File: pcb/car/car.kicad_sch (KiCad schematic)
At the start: 9 parts

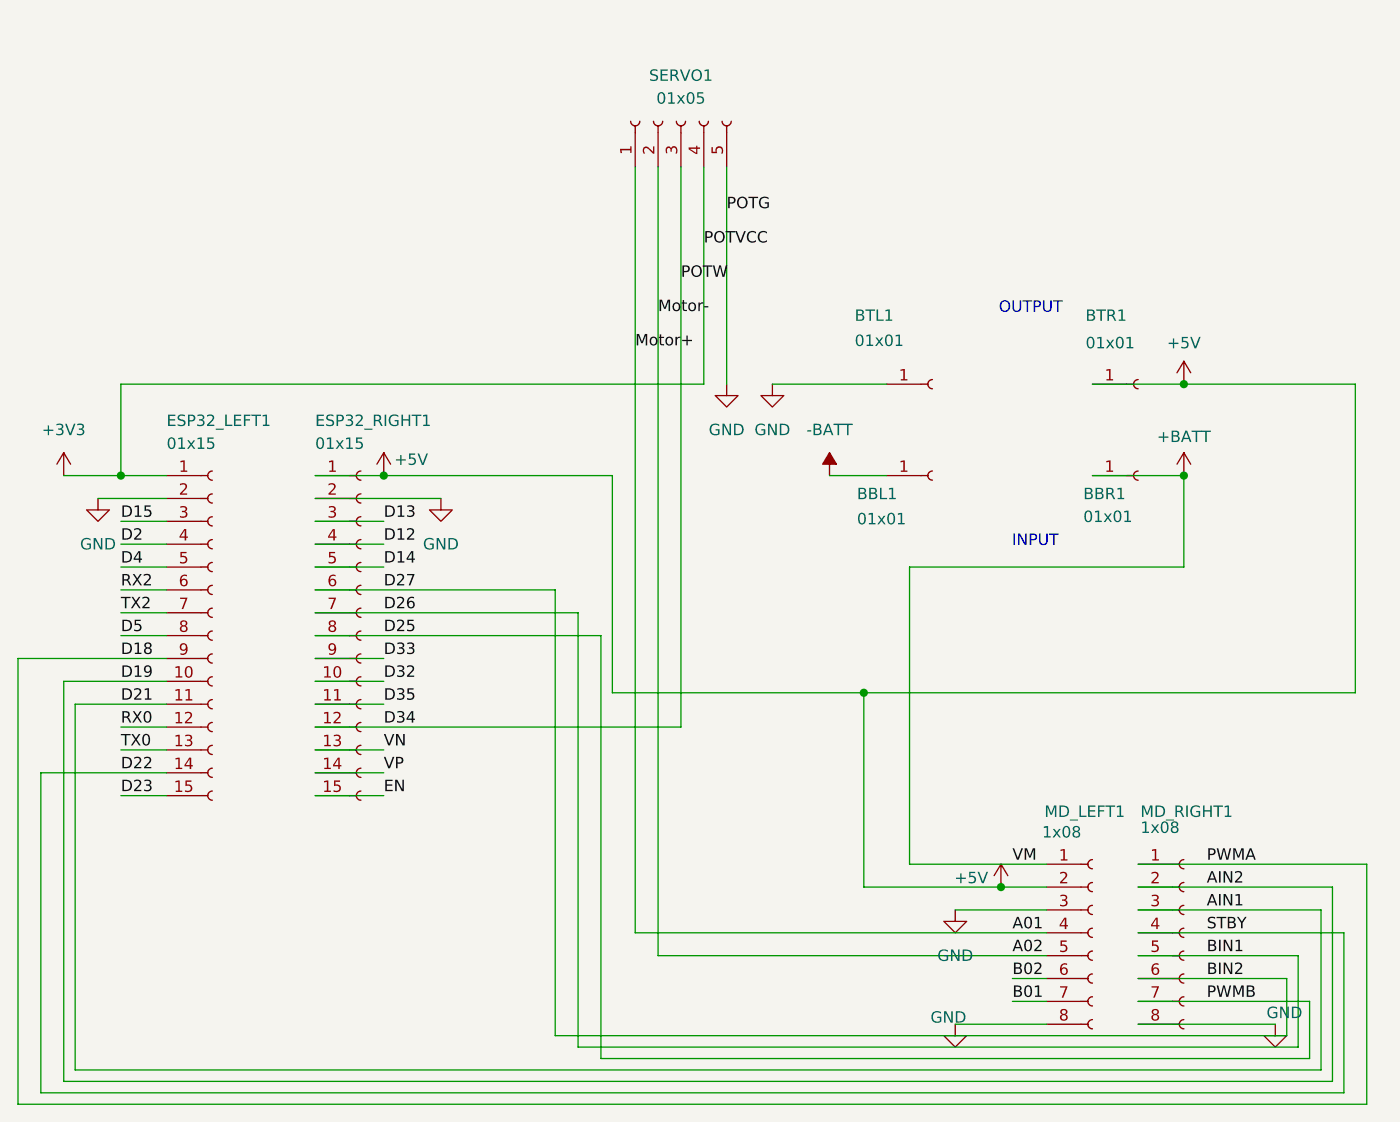
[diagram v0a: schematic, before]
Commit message: feat: clean up and adding mpu6050
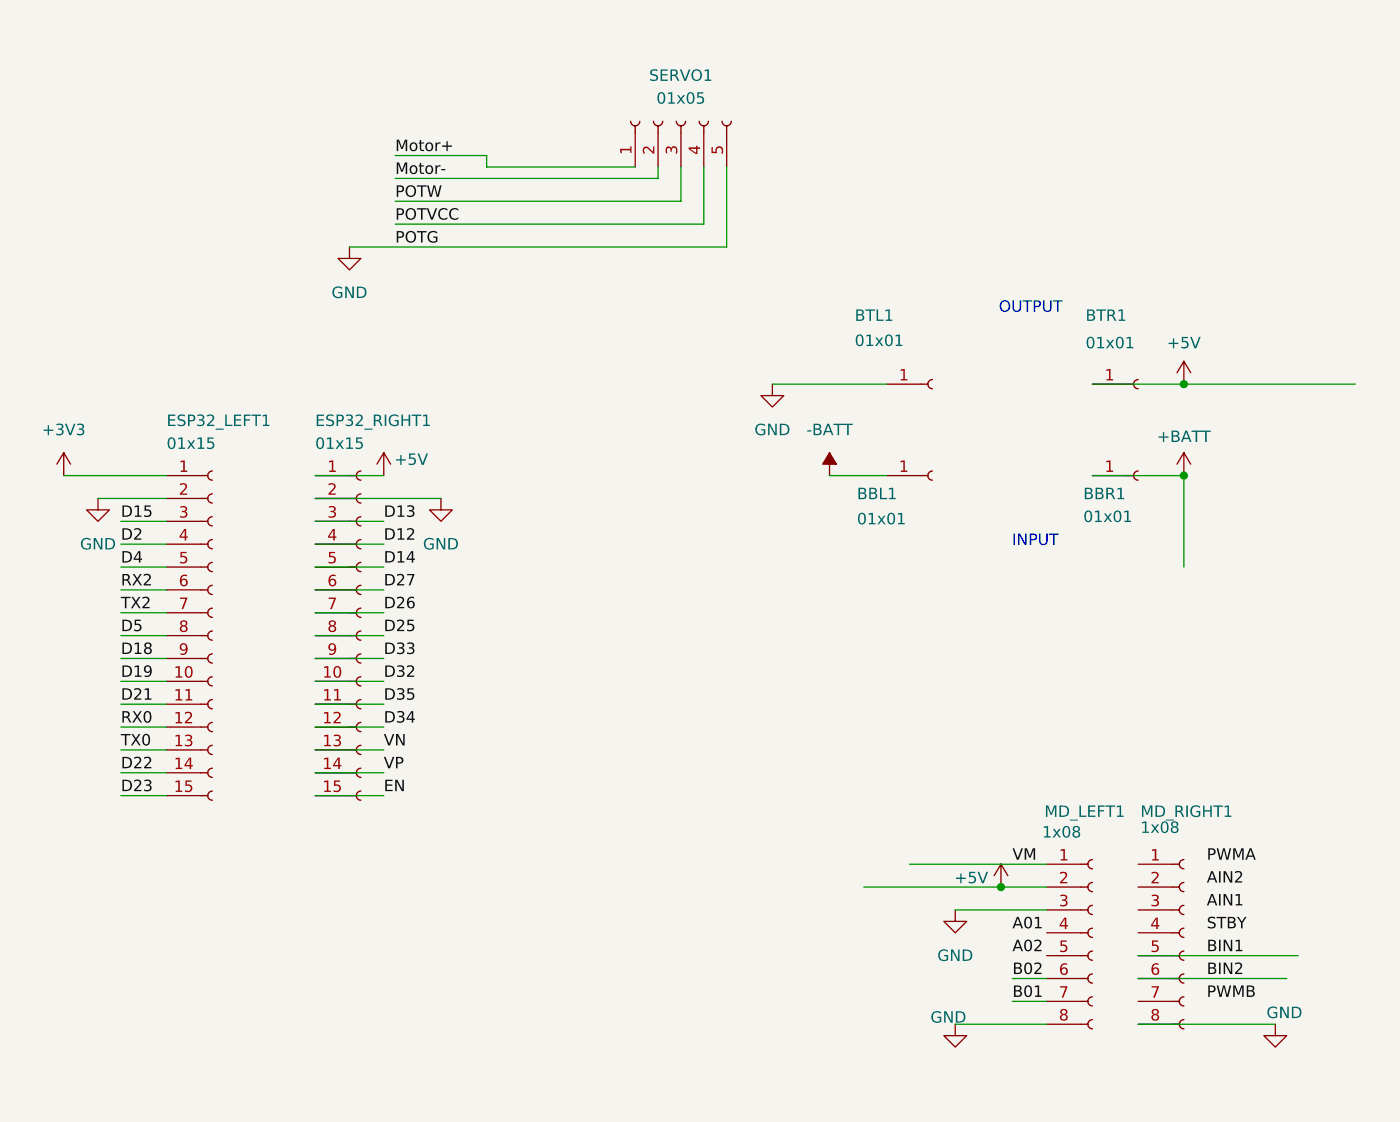
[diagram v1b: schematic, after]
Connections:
- net +3V3: no longer SERVO1.4 (Pin_4)
- net +BATT: no longer MD_LEFT1.1 (Pin_1)
- net A01: no longer MD_LEFT1.4 (Pin_4), SERVO1.1 (Pin_1)
- net A02: no longer MD_LEFT1.5 (Pin_5), SERVO1.2 (Pin_2)
- net AIN1: no longer ESP32_LEFT1.11 (Pin_11), MD_RIGHT1.3 (Pin_3)
- net AIN2: no longer ESP32_LEFT1.10 (Pin_10), MD_RIGHT1.2 (Pin_2)
- net BIN1: no longer ESP32_RIGHT1.7 (Pin_7)
- net BIN2: no longer ESP32_RIGHT1.6 (Pin_6)
- net D18: no longer MD_RIGHT1.1 (Pin_1)
- net D22: no longer MD_RIGHT1.4 (Pin_4)
- net D25: no longer MD_RIGHT1.7 (Pin_7)
- net D34: no longer SERVO1.3 (Pin_3)
- new net D19: ESP32_LEFT1.10 (Pin_10)
- new net D21: ESP32_LEFT1.11 (Pin_11)
- new net D26: ESP32_RIGHT1.7 (Pin_7)
- new net D27: ESP32_RIGHT1.6 (Pin_6)
- new net Motor+: SERVO1.1 (Pin_1)
- new net Motor-: SERVO1.2 (Pin_2)
- new net POTVCC: SERVO1.4 (Pin_4)
- new net POTW: SERVO1.3 (Pin_3)
- new net VM: MD_LEFT1.1 (Pin_1)

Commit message: feat: cleaning up pdb
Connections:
- net -BATT is gone; now on net GND: BBL1.1 (Pin_1)
- net B02 is gone; now on net GND: MD_LEFT1.6 (Pin_6)
- net D18 is gone; now on net AIN1: ESP32_LEFT1.9 (Pin_9)
- net D21 is gone; now on net BIN1: ESP32_LEFT1.11 (Pin_11)
- net D22 is gone; now on net BIN2: ESP32_LEFT1.14 (Pin_14)
- net D27 is gone; now on net AIN2: ESP32_RIGHT1.6 (Pin_6)
- net Motor+ is gone; now on net GND: SERVO1.1 (Pin_1)
- net Motor- is gone; now on net +3.3V: SERVO1.2 (Pin_2)
- net POTVCC is gone; now on net +: SERVO1.4 (Pin_4)
- net POTW is gone; now on net D33: SERVO1.3 (Pin_3)
- net VM is gone; now on net +BATT: MD_LEFT1.1 (Pin_1)
- net A01: now also MD_LEFT1.4 (Pin_4)
- net A02: now also MD_LEFT1.5 (Pin_5)
- net AIN1: now also MD_RIGHT1.3 (Pin_3)
- net AIN2: now also MD_RIGHT1.2 (Pin_2)
- net D14: now also MD_RIGHT1.1 (Pin_1)
- net D19: now also MD_RIGHT1.4 (Pin_4)
- net D23: now also MD_RIGHT1.7 (Pin_7)
- net +3V3 renamed +3.3V
- net B01 renamed +
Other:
- moved on the sheet: BBL1, BBR1, BTL1, BTR1, ESP32_LEFT1, ESP32_RIGHT1, MD_LEFT1, MD_RIGHT1, SERVO1

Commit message: feat: cleaning up pcb
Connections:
- net A01 is gone; now on net D19: MD_LEFT1.4 (Pin_4)
- net A02 is gone; now on net BIN1: MD_LEFT1.5 (Pin_5)
- net +: now also MD_RIGHT1.4 (Pin_4); no longer MD_LEFT1.7 (Pin_7)
- net +5V: now also MD_RIGHT1.2 (Pin_2); no longer MD_LEFT1.2 (Pin_2)
- net +BATT: now also MD_RIGHT1.1 (Pin_1); no longer MD_LEFT1.1 (Pin_1)
- net AIN1: now also ESP32_LEFT1.11 (Pin_11), MD_LEFT1.3 (Pin_3); no longer ESP32_LEFT1.9 (Pin_9), MD_RIGHT1.3 (Pin_3)
- net AIN2: now also ESP32_LEFT1.14 (Pin_14), MD_LEFT1.2 (Pin_2); no longer ESP32_RIGHT1.6 (Pin_6), MD_RIGHT1.2 (Pin_2)
- net BIN1: now also ESP32_LEFT1.9 (Pin_9); no longer ESP32_LEFT1.11 (Pin_11), MD_RIGHT1.5 (Pin_5)
- net BIN2: now also ESP32_RIGHT1.6 (Pin_6), MD_LEFT1.6 (Pin_6); no longer ESP32_LEFT1.14 (Pin_14), MD_RIGHT1.6 (Pin_6)
- net D14: now also MD_LEFT1.7 (Pin_7); no longer MD_RIGHT1.1 (Pin_1)
- net D19: no longer MD_RIGHT1.4 (Pin_4)
- net D23: now also MD_LEFT1.1 (Pin_1); no longer MD_RIGHT1.7 (Pin_7)
- net GND: now also MD_RIGHT1.3 (Pin_3), MD_RIGHT1.5 (Pin_5), MD_RIGHT1.6 (Pin_6); no longer MD_LEFT1.3 (Pin_3), MD_LEFT1.6 (Pin_6)
- new net B1: MD_RIGHT1.7 (Pin_7)

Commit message: feat: update pcb, update car code
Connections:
- net +3.3V: now also ESP32_RIGHT1.9 (Pin_9); no longer ESP32_LEFT1.1 (Pin_1)
- net GND: no longer MD_RIGHT1.5 (Pin_5), MD_RIGHT1.6 (Pin_6), SERVO1.5 (Pin_5)
- net D33 renamed +3V3
- net +3V3: now also ESP32_LEFT1.1 (Pin_1); no longer ESP32_RIGHT1.9 (Pin_9)
- new net -: MD_RIGHT1.5 (Pin_5), SERVO1.5 (Pin_5)
